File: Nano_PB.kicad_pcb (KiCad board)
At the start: 2 copper layers, 100 x 50 mm, 129 parts, among them CON1 BARREL_JACK, P1 CONN_02X04, P10 CONN_01X04, P11 CONN_01X04, P12 CONN_01X04, P2 CONN_01X06, P3 CONN_01X01, P4 CONN_01X03, P5 CONN_01X03, P6 CONN_01X03, P7 CONN_01X03, P8 CONN_01X03, P9 CONN_01X04, Q1 SMBT3904, Q2 SMBT3904, Q3 SMBT3904, Q4 SMBT3904, Q5 SMBT3904, Q6 BSS138, Q7 BSS138, SW1 Izquierda, SW2 Arriba, SW3 Abajo, SW4 Derecha, U1 Arduino_Nano, U2 LM7805CT, U3 74HC595, U4 74HC595, U5 Matriz_5x7, U6 PCA9551, U7 74HC148, U8 MMA7660FC, U9 40106

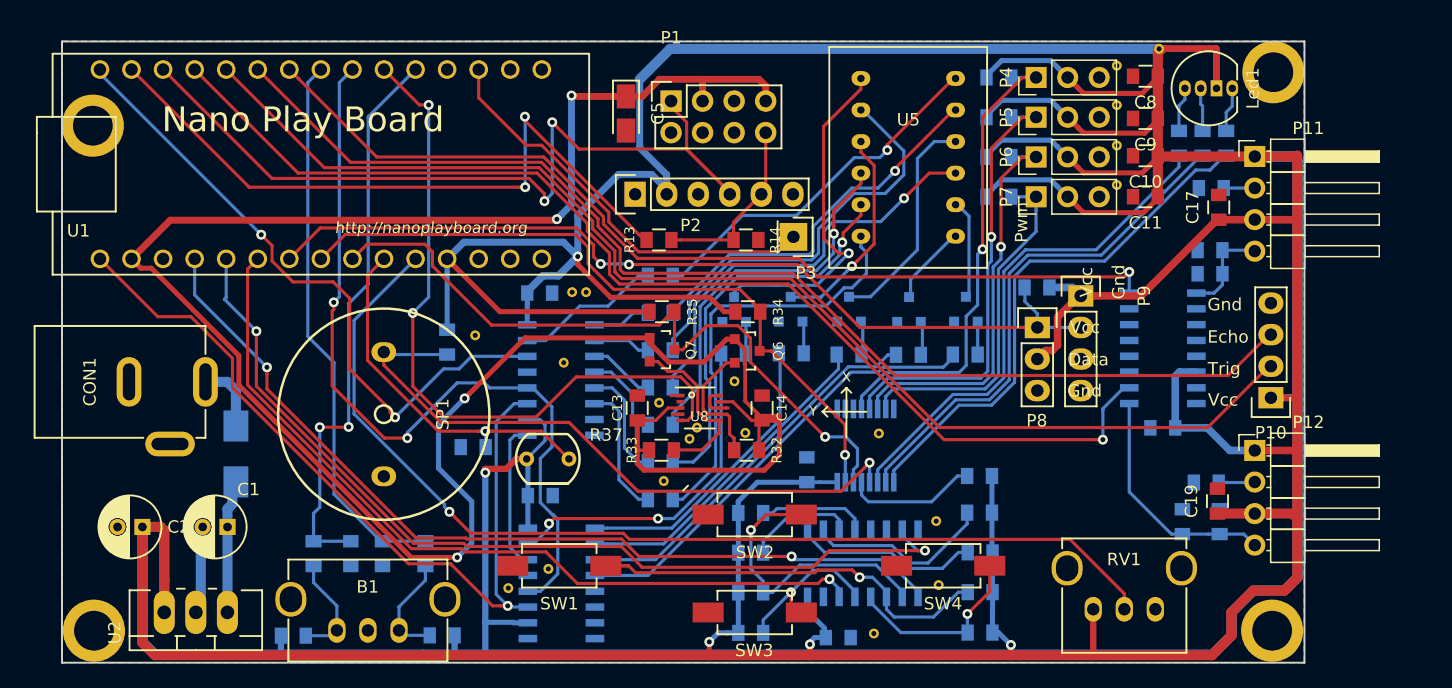
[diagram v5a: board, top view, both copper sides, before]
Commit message: corregida serigrafia inferior
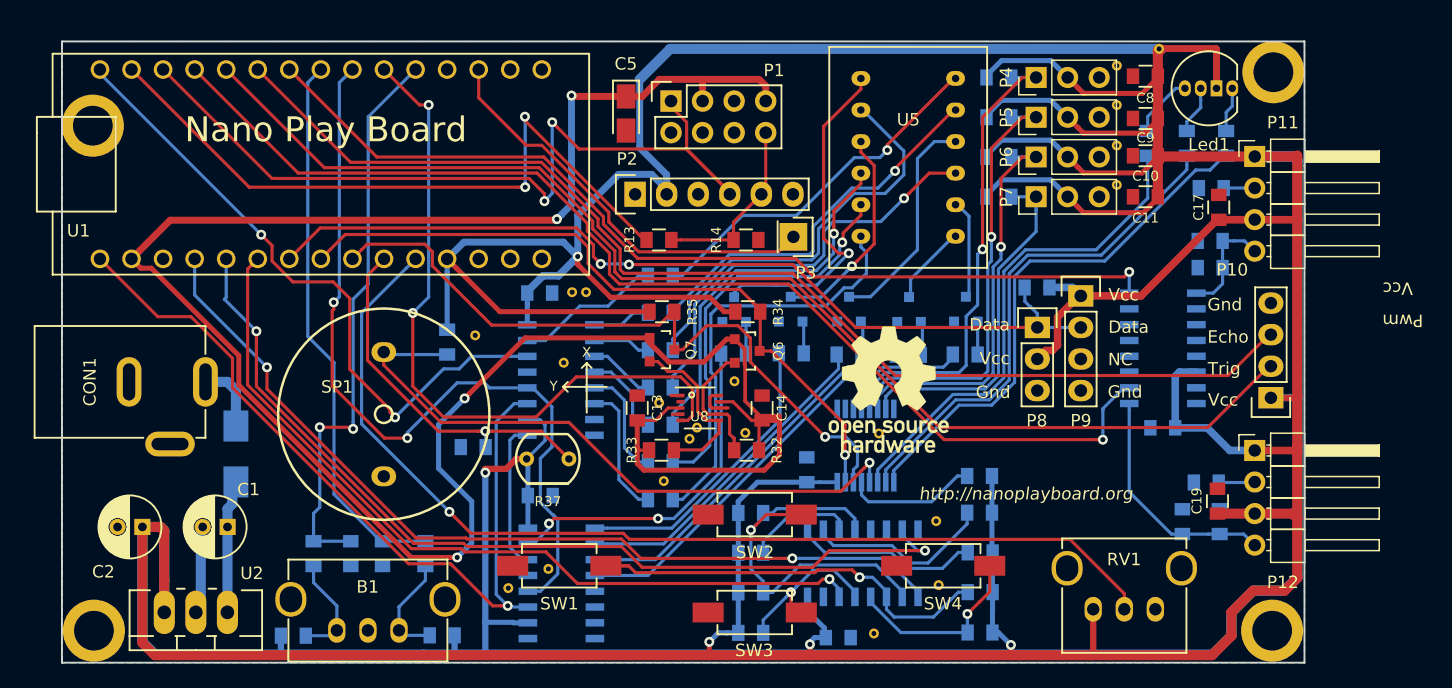
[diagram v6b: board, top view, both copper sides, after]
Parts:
- added G***: KiCad Logo, logos:KiCad-Logo_11mmx5mm, B.Cu at (62.1, 34.9)
- added G***: LOGO, logos:osh-logo, F.Cu at (118.6, 52.8)
- added G***: LOGO, logos:logo_HackLabAl, B.Cu at (81.4, 35.4)
- moved R21 2.52 mm to (139.5, 33.0)
- moved R22 1.27 mm to (142.6, 33.0)
- moved R44 0.75 mm to (144.5, 40.8)
- moved C18 0.50 mm to (144.5, 43.0)
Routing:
- net Net-(Led1-Pad1): track 3.62 -> 5.10 mm
- net Net-(C18-Pad1): track 7.79 -> 8.92 mm
- net LED_GREEN: track 41.3 -> 40.2 mm
- net LED_BLUE: track 42.0 -> 41.4 mm
- net A7: track 83.9 -> 83.4 mm
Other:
- board text added: "01/17"
- board text added: "Buzz-Ch8"
- board text added: "Ch 1"
- board text added: "Ch 2"
- board text added: "Ch 3"
- board text added: "Ch 4"
- board text added: "Dcha-D9"
- board text added: "E+"
- board text added: "E-"
- board text added: "Izq-D6"
- board text added: "NC"
- board text added: "R+"
- board text added: "R-"
- board text added: "Rev-0.3.0"
- board text added: "Rst"
- board text removed: "10/16"
- board text removed: "Buzz-D3"
- board text removed: "Reset"
- board text removed: "Rev-0.2.1"
- board text removed: "Servo 1"
- board text removed: "Servo 2"

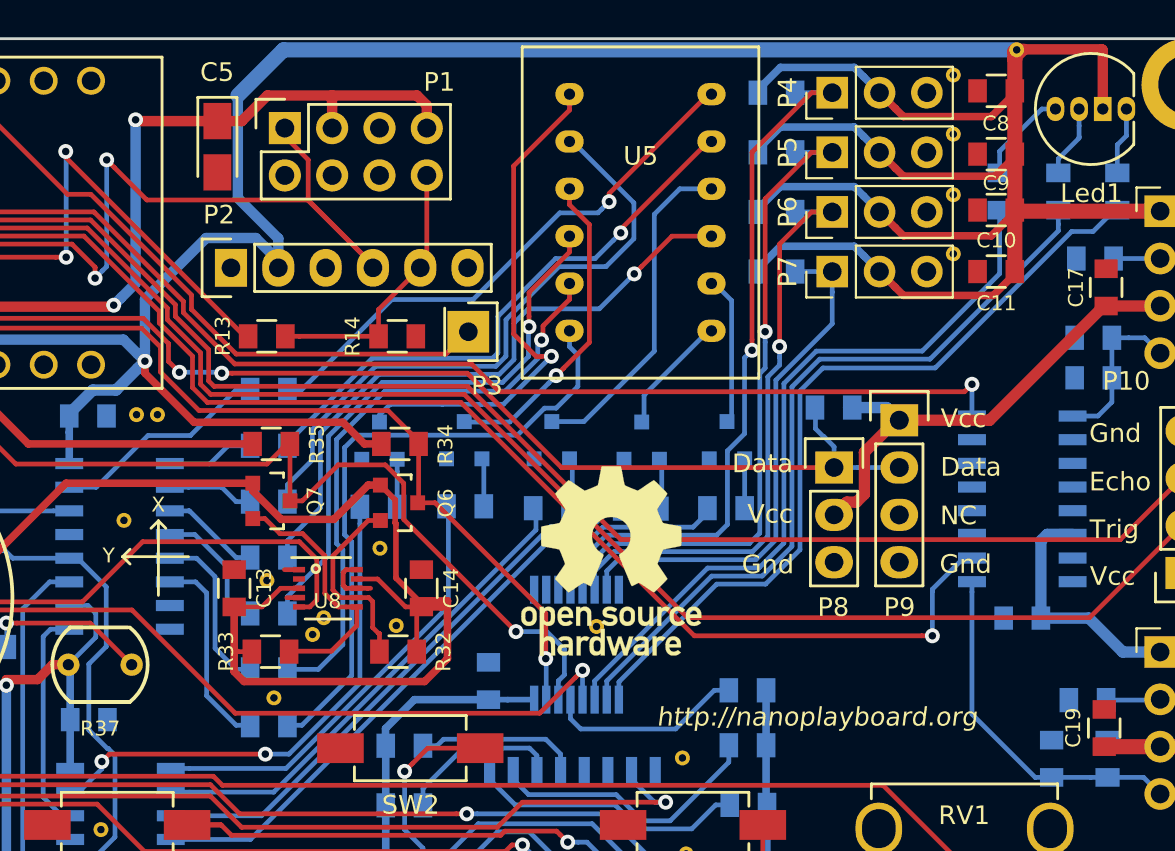
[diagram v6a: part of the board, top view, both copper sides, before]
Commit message: modificada posicion del modulo esp
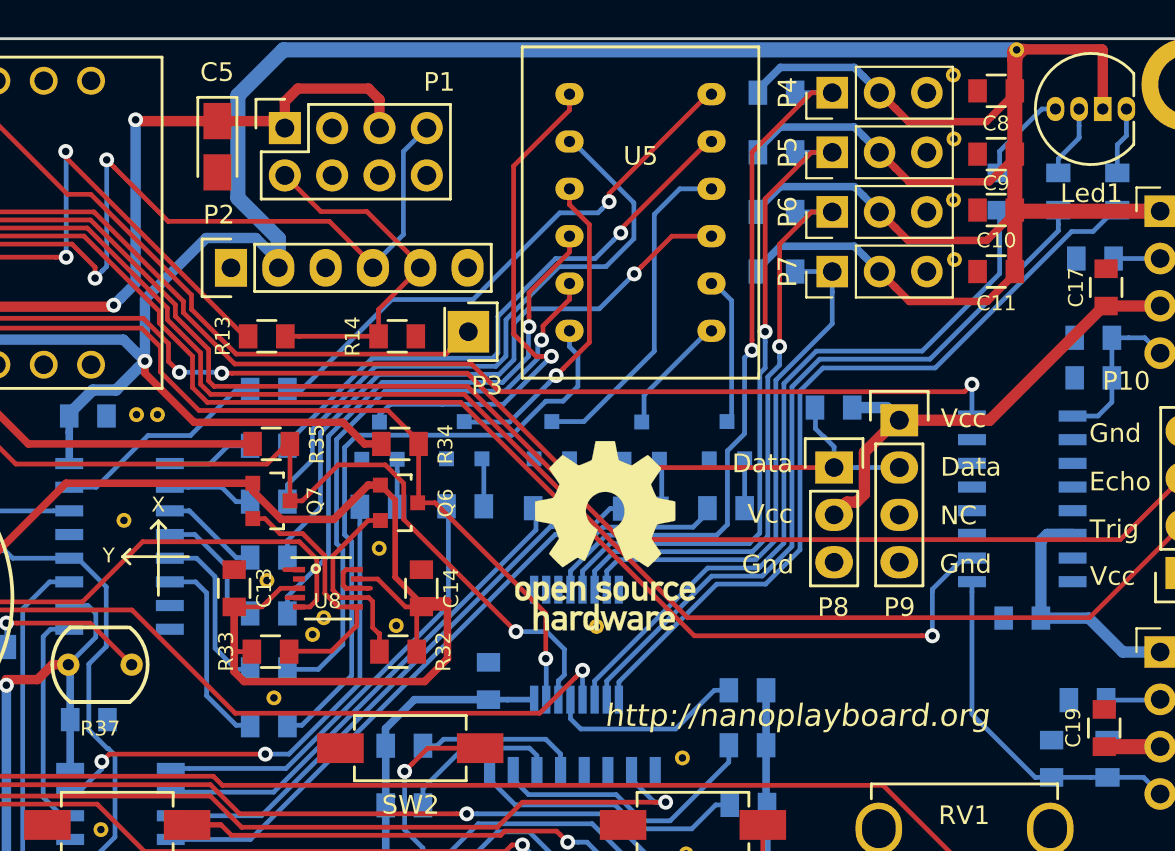
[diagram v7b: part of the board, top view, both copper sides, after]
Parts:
- moved G*** 1.39 mm to (118.3, 51.5)
- moved Gnd-Via 0.31 mm to (137.1, 36.6)
- moved Gnd-Via 0.28 mm to (137.0, 33.4)
- moved Gnd-Via 0.26 mm to (137.0, 30.1)
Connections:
- P1 pad 1: D10 -> +3V3
- P1 pad 2: GND -> /Bluetooth/RxD
- P1 pad 3: +3V3 -> Net-(P1-Pad3)
- P1 pad 5: Net-(P1-Pad5) -> +3V3
- P1 pad 7: +3V3 -> D10
- P1 pad 8: /Bluetooth/RxD -> GND
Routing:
- net /Bluetooth/RxD: track 14.7 -> 19.5 mm
- net +3V3: track 184.2 -> 182.0 mm
- net +5V: track 669.6 -> 670.7 mm
- net D10: track 68.1 -> 67.5 mm

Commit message: modificaciones menores en el trazado para optimizarlo
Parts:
- added Gnd-Via: VAL**, Vias:Gnd-Via, F.Cu at (64.1, 40.6)
- added Gnd-Via: VAL**, Vias:Gnd-Via, F.Cu at (103.7, 58.4)
- moved R36 0.83 mm to (83.1, 48.1)
- moved R23 0.67 mm to (130.7, 45.2)
- moved C9 0.13 mm to (139.3, 30.8)
- moved P10 0.10 mm to (149.3, 53.5)
- turned C1 to 0 degrees
- turned C2 to 0 degrees
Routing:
- net +5V: track 670.7 -> 697.7 mm, vias 5 -> 2
- net A2: track 65.8 -> 76.0 mm
- net D5: track 44.4 -> 51.5 mm
- net D7: track 94.5 -> 101.0 mm
- net D2: track 46.1 -> 51.0 mm
- net A0: track 72.5 -> 76.0 mm
- net D8: track 99.4 -> 101.1 mm
- net A1: track 74.6 -> 76.0 mm
- net D10: track 67.5 -> 68.7 mm
- net RESET: track 33.7 -> 33.0 mm
- net Net-(R4-Pad1): track 33.9 -> 34.6 mm
- net Net-(R3-Pad1): track 33.8 -> 34.4 mm
- net A4: track 56.9 -> 57.4 mm
- net Net-(R6-Pad1): track 32.0 -> 31.5 mm
